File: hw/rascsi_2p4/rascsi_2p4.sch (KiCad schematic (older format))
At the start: 123 parts, among them IC1 SN74LS641-1DW, IC2 SN74LS641-1DW, IC3 SN74LS641-1DW, IC4 SN74LS641-1DW, J1 Raspberry_Pi_2_3, J2 DNP, J4 I2C Pinout, J5 DNP, J6 CONNFLY DB-25, J7 DNP, U1 74ALVC164245DGG, U2 74ALVC164245DGG, X1 Mac, X2 Dogcow, X3 Mac, X4 Dogcow, X5 Dogcow, X6 Dogcow, X7 Pi, X8 Pi

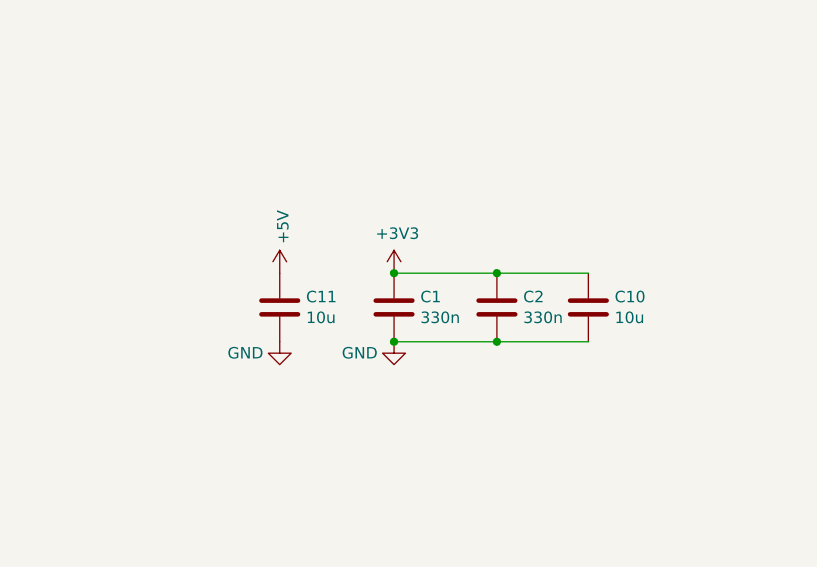
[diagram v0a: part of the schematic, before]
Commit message: added U1/U2 caps for 3.3V
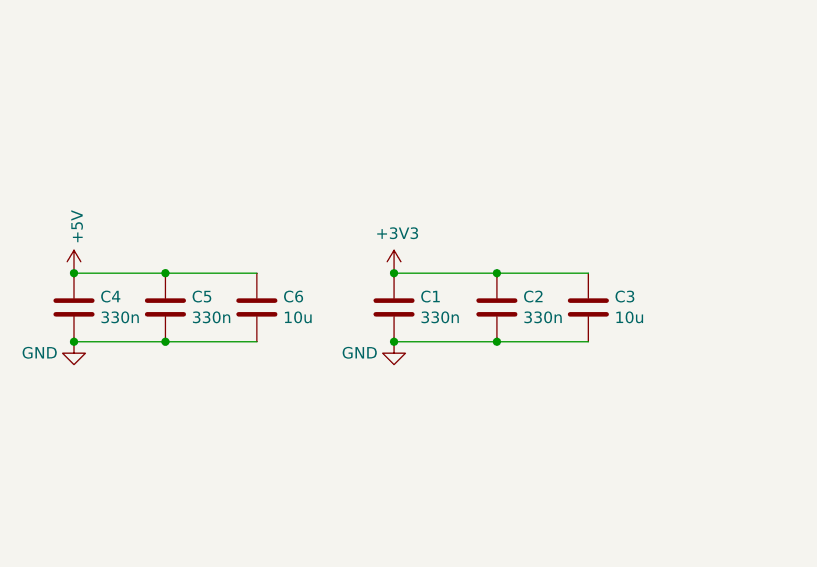
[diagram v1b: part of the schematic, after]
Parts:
- added C4, C5: 330n, Capacitor_SMD:C_0805_2012Metric, symbol Device:C
- renumbered C10 to C3, C11 to C6
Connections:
- net +5V: now also C4.1, C5.1
- net GND: now also C4.2, C5.2
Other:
- moved on the sheet: C6
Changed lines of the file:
@@
 $EndComp
 $Comp
-L Device:C C10
+L Device:C C3
 U 1 1 62197548
 P 1150 10000
-F 0 "C10" H 1265 10046 50  0000 L CNN
+F 0 "C3" H 1265 10046 50  0000 L CNN
 F 1 "10u" H 1265 9955 50  0000 L CNN
 F 2 "Capacitor_SMD:C_0805_2012Metric" H 1188 9850 50  0001 C CNN
@@
 $EndComp
 $Comp
-L Device:C C11
+L Device:C C6
 U 1 1 6219855C
-P -200 10000
-F 0 "C11" H -85 10046 50  0000 L CNN
-F 1 "10u" H -85 9955 50  0000 L CNN
-F 2 "Capacitor_SMD:C_0805_2012Metric" H -162 9850 50  0001 C CNN
-F 3 "https://datasheet.lcsc.com/szlcsc/Samsung-Electro-Mechanics-CL21A106KAYNNNE_C15850.pdf" H -200 10000 50  0001 C CNN
-F 4 "C15850" H -200 10000 50  0001 C CNN "LCSC"
-F 5 "Samsung Electro-Mechanics" H -200 10000 50  0001 C CNN "Manufacturer_Name"
-F 6 "CL21A106KAYNNNE" H -200 10000 50  0001 C CNN "Manufacturer_Part_Number"
-	1    -200 10000
+P -300 10000
+F 0 "C6" H -185 10046 50  0000 L CNN
+F 1 "10u" H -185 9955 50  0000 L CNN
+F 2 "Capacitor_SMD:C_0805_2012Metric" H -262 9850 50  0001 C CNN
+F 3 "https://datasheet.lcsc.com/szlcsc/Samsung-Electro-Mechanics-CL21A106KAYNNNE_C15850.pdf" H -300 10000 50  0001 C CNN
+F 4 "C15850" H -300 10000 50  0001 C CNN "LCSC"
+F 5 "Samsung Electro-Mechanics" H -300 10000 50  0001 C CNN "Manufacturer_Name"
+F 6 "CL21A106KAYNNNE" H -300 10000 50  0001 C CNN "Manufacturer_Part_Number"
+	1    -300 10000
 	1    0    0    -1
 $EndComp
 $Comp
-L power:GND #PWR?
+L power:GND #PWR0105
 U 1 1 62199FF5
 P 300 10150
-F 0 "#PWR?" H 300 9900 50  0001 C CNN
+F 0 "#PWR0105" H 300 9900 50  0001 C CNN
 F 1 "GND" H 150 10100 50  0000 C CNN
 F 2 "" H 300 10150 50  0001 C CNN
@@
 $EndComp
 $Comp
-L power:GND #PWR?
+L power:GND #PWR0106
 U 1 1 621E9490
-P -200 10150
-F 0 "#PWR?" H -200 9900 50  0001 C CNN
-F 1 "GND" H -350 10100 50  0000 C CNN
-F 2 "" H -200 10150 50  0001 C CNN
-F 3 "" H -200 10150 50  0001 C CNN
-	1    -200 10150
+P -1100 10150
+F 0 "#PWR0106" H -1100 9900 50  0001 C CNN
+F 1 "GND" H -1250 10100 50  0000 C CNN
+F 2 "" H -1100 10150 50  0001 C CNN
+F 3 "" H -1100 10150 50  0001 C CNN
+	1    -1100 10150
 	1    0    0    -1
 $EndComp
 $Comp
-L power:+3V3 #PWR?
+L power:+3V3 #PWR0107
 U 1 1 622100B8
 P 300 9850
-F 0 "#PWR?" H 300 9700 50  0001 C CNN
+F 0 "#PWR0107" H 300 9700 50  0001 C CNN
 F 1 "+3V3" H 315 10023 50  0000 C CNN
 F 2 "" H 300 9850 50  0001 C CNN
@@
 $EndComp
 $Comp
-L power:+5V #PWR?
+L power:+5V #PWR0108
 U 1 1 62210F2C
-P -200 9850
-F 0 "#PWR?" H -200 9700 50  0001 C CNN
-F 1 "+5V" V -185 9978 50  0000 L CNN
-F 2 "" H -200 9850 50  0001 C CNN
-F 3 "" H -200 9850 50  0001 C CNN
-	1    -200 9850
+P -1100 9850
+F 0 "#PWR0108" H -1100 9700 50  0001 C CNN
+F 1 "+5V" V -1085 9978 50  0000 L CNN
+F 2 "" H -1100 9850 50  0001 C CNN
+F 3 "" H -1100 9850 50  0001 C CNN
+	1    -1100 9850
 	1    0    0    -1
 $EndComp
@@
 	750  10150 1150 10150
 Connection ~ 750  10150
+$Comp
+L Device:C C4
+U 1 1 62625777
+P -1100 10000
+F 0 "C4" H -985 10046 50  0000 L CNN
+F 1 "330n" H -985 9955 50  0000 L CNN
+F 2 "Capacitor_SMD:C_0805_2012Metric" H -1062 9850 50  0001 C CNN
+F 3 "https://datasheet.lcsc.com/szlcsc/Guangdong-Fenghua-Advanced-Tech-0805B334K500NT_C1740.pdf" H -1100 10000 50  0001 C CNN
+F 4 "C1740" H -1100 10000 50  0001 C CNN "LCSC"
+F 5 "Guangdong Fenghua Advanced Tech" H -1100 10000 50  0001 C CNN "Manufacturer_Name"
+F 6 "0805B334K500NT" H -1100 10000 50  0001 C CNN "Manufacturer_Part_Number"
+	1    -1100 10000
+	1    0    0    -1
+$EndComp
+$Comp
+L Device:C C5
+U 1 1 62625CE2
+P -700 10000
+F 0 "C5" H -585 10046 50  0000 L CNN
+F 1 "330n" H -585 9955 50  0000 L CNN
+F 2 "Capacitor_SMD:C_0805_2012Metric" H -662 9850 50  0001 C CNN
+F 3 "https://datasheet.lcsc.com/szlcsc/Guangdong-Fenghua-Advanced-Tech-0805B334K500NT_C1740.pdf" H -700 10000 50  0001 C CNN
+F 4 "C1740" H -700 10000 50  0001 C CNN "LCSC"
+F 5 "Guangdong Fenghua Advanced Tech" H -700 10000 50  0001 C CNN "Manufacturer_Name"
+F 6 "0805B334K500NT" H -700 10000 50  0001 C CNN "Manufacturer_Part_Number"
+	1    -700 10000
+	1    0    0    -1
+$EndComp
+Wire Wire Line
+	-700 9850 -1100 9850
+Connection ~ -1100 9850
+Wire Wire Line
+	-700 9850 -300 9850
+Connection ~ -700 9850
+Wire Wire Line
+	-700 10150 -1100 10150
+Connection ~ -1100 10150
+Wire Wire Line
+	-700 10150 -300 10150
+Connection ~ -700 10150
 $EndSCHEMATC

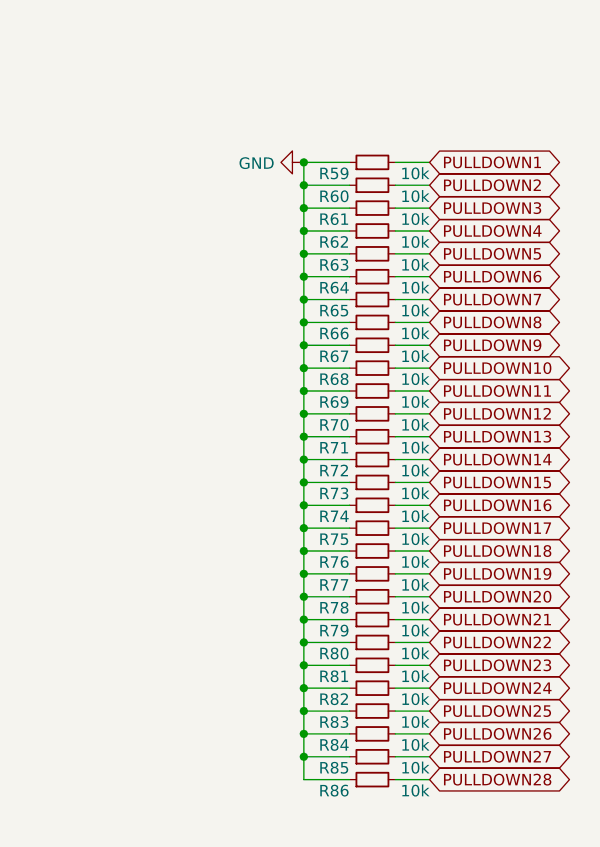
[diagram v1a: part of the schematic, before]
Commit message: replaced R59-R86 by 100k to reduce power dissipation
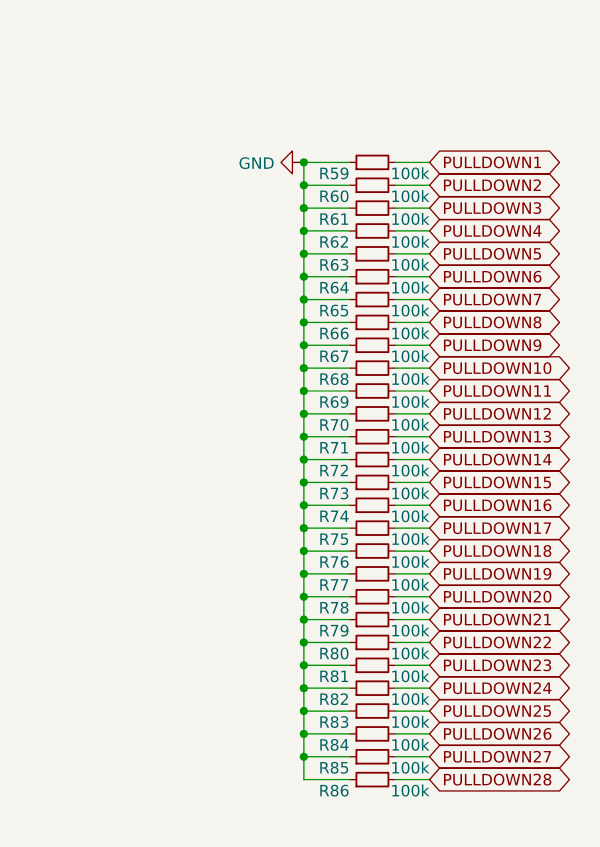
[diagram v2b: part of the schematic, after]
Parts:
- R59, R60, R61, R62, R63, R64, R65, R66, R67, R68, R69, R70, R71, R72, R73, R74, R75, R76, R77, R78, R79, R80, R81, R82, R83, R84, R85, R86: value 10k -> 100k; Description Chip Resistor - Surface Mount 10KOhms ±1% 1/16W 0402 RoHS -> Chip Resistor - Surface Mount 100KOhms ±1% 1/16W 0402 RoHS; LCSC C25744 -> C25741; Manufacturer_Part_Number 0402WGF1002TCE -> 0402WGF1003TCE

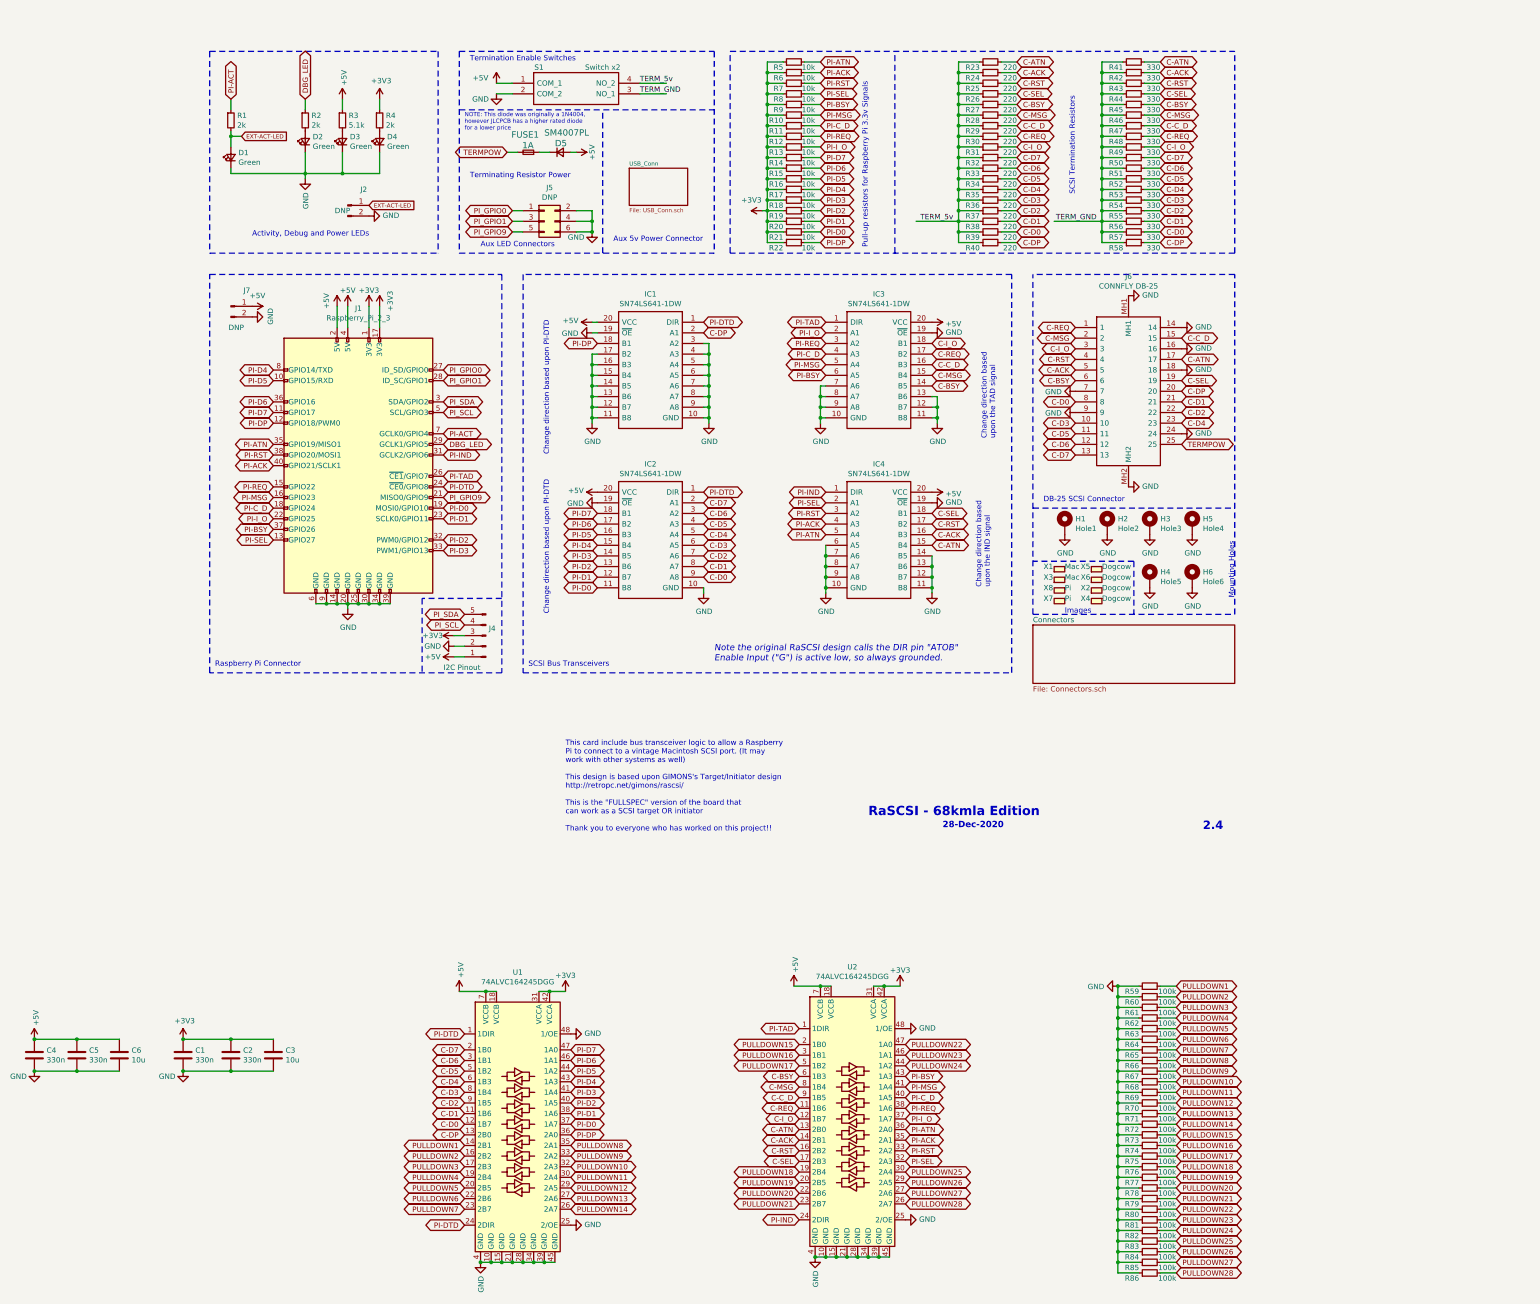
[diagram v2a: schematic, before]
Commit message: use active SCSI termination
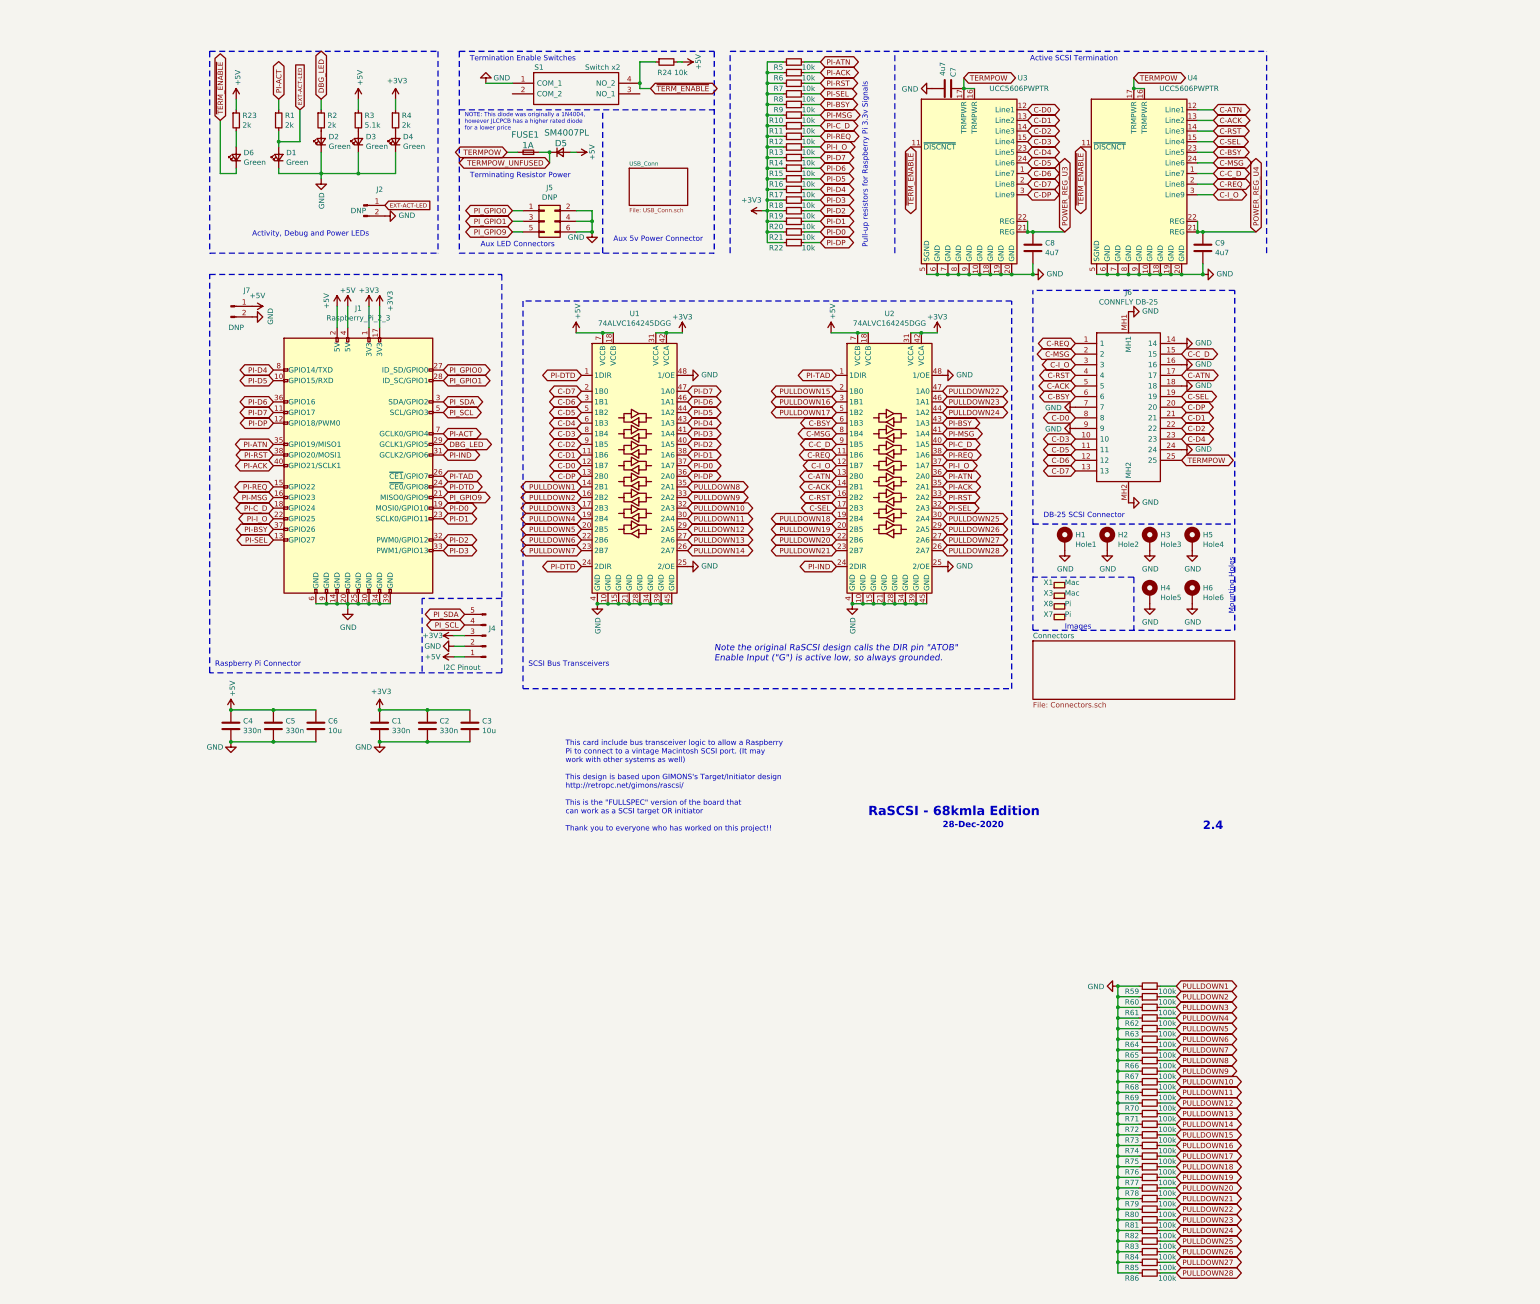
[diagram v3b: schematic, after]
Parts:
- removed IC1, IC2, IC3, IC4: SN74LS641-1DW, SamacSys_Parts:SOIC127P1030X265-20N, symbol SamacSys_Parts:SN74LS245DW
- removed R25, R26, R27, R28, R29, R30, R31, R32, R33, R34, R35, R36, R37, R38, R39, R40: 220, Resistor_SMD:R_0402_1005Metric, symbol Device:R_Small
- removed R41, R42, R43, R44, R45, R46, R47, R48, R49, R50, R51, R52, R53, R54, R55, R56, R57, R58: 330, Resistor_SMD:R_0402_1005Metric, symbol Device:R_Small
- removed X2, X4, X5, X6: Dogcow, SamacSys_Parts:dogcow, symbol SamacSys_Parts:Logo
- added C7, C8, C9: 4u7, Capacitor_SMD:C_0805_2012Metric, symbol Device:C
- added D6: Green, LED_SMD:LED_0805_2012Metric, symbol Device:LED_Small
- added U3, U4: UCC5606PWPTR, Package_SO:TSSOP-24_6.1x7.8mm_P0.65mm, symbol amiga:UCC5606PWPTR
- R23: value 220 -> 2k; Description 220Ω ±1% 1/16W ±100ppm/℃ 0402 Chip Resistor -> 2kΩ ±1% 1/16W ±100ppm/℃ 0402 Chip Resistor; LCSC C25091 -> C4109; Manufacturer_Part_Number 0402WGF2200TCE -> 0402WGF2001TCE
- R24: value 220 -> 10k; Description 220Ω ±1% 1/16W ±100ppm/℃ 0402 Chip Resistor -> 10kΩ ±1% 1/16W ±100ppm/℃ 0402 Chip Resistor; LCSC C25091 -> C25744; Manufacturer_Part_Number 0402WGF2200TCE -> 0402WGF1002TCE
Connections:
- net +5V: now also R23.1, R24.2; no longer S1.1 (COM_1)
- net C-ACK: now also U4.13 (Line2); no longer R24.2
- net C-ATN: now also U4.12 (Line1); no longer R23.2
- net C-BSY: now also U4.23 (Line5)
- net C-C_D: now also U4.1 (Line7)
- net C-D0: now also U3.12 (Line1)
- net C-D1: now also U3.13 (Line2)
- net C-D2: now also U3.14 (Line3)
- net C-D3: now also U3.15 (Line4)
- net C-D4: now also U3.23 (Line5)
- net C-D5: now also U3.24 (Line6)
- net C-D6: now also U3.1 (Line7)
- net C-D7: now also U3.2 (Line8)
- net C-DP: now also U3.3 (Line9)
- net C-I_O: now also U4.3 (Line9)
- net C-MSG: now also U4.24 (Line6)
- net C-REQ: now also U4.2 (Line8)
- net C-RST: now also U4.14 (Line3)
- net C-SEL: now also U4.15 (Line4)
- net GND: now also S1.1 (COM_1), C7.2, C8.2, C9.2, U3.10 (GND), U3.18 (GND), U3.19 (GND), U3.20 (GND), U3.5 (SGND), U3.6 (GND), U3.7 (GND), U3.8 (GND), U3.9 (GND), U4.10 (GND), U4.18 (GND), U4.19 (GND), U4.20 (GND), U4.5 (SGND), U4.6 (GND), U4.7 (GND), U4.8 (GND), U4.9 (GND); no longer S1.2 (COM_2)
- net TERMPOW: now also C7.1, U3.16 (TRMPWR), U3.17 (TRMPWR), U4.16 (TRMPWR), U4.17 (TRMPWR)
- net TERMPOW_UNFUSED: now reaches D5.1 (K), FUSE1.1
- net TERM_5v renamed ~TERM_ENABLE
- net ~TERM_ENABLE: now also D6.1 (K), U3.11 (~DISCNCT), U4.11 (~DISCNCT); no longer R23.1
- net TERM_GND: no longer names the net of S1.3 (NO_1)
- new net: D6.2 (A), R23.2
- new net POWER_REG_U3: C8.1, U3.21 (REG), U3.22 (REG)
- new net POWER_REG_U4: C9.1, U4.21 (REG), U4.22 (REG)
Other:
- note added: "Active SCSI Termination"
- note removed: "Change direction based \nupon the IND signal"
- note removed: "Change direction based \nupon the TAD signal"
- note removed: "Change direction based upon PI-DTD"
- note removed: "SCSI Termination Resistors"
- moved on the sheet: C1, C2, C3, C4, C5, C6, D1, D2, D3, D4, H1, H2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
